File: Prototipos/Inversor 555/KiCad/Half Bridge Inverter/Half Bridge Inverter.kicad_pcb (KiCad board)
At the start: 2 copper layers, 91 x 53.5 mm, 15 parts, among them Q1 CSD18534Q5A, Q2 CSD18534Q5A, Q3 BC548, U1 TLC555xD, U2 LM7809_TO220

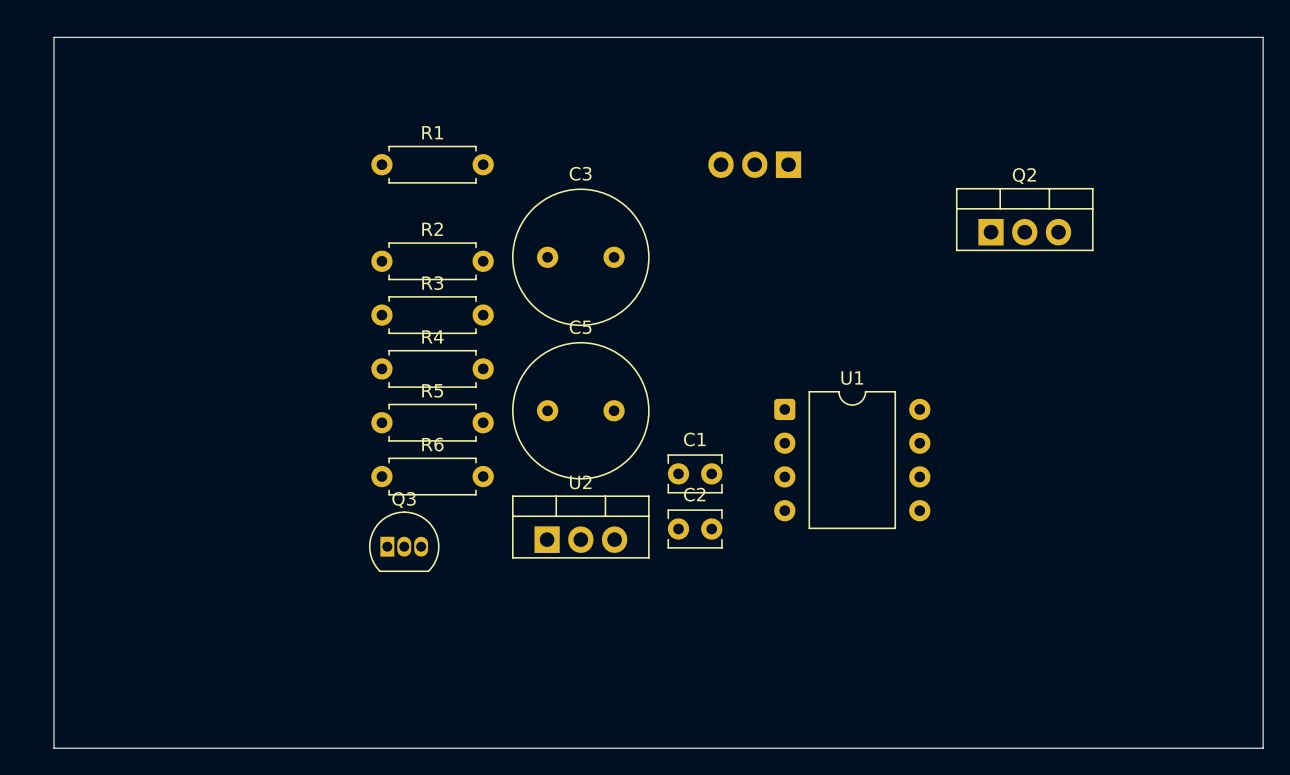
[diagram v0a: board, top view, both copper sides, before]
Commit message: Agregar diseño PCB
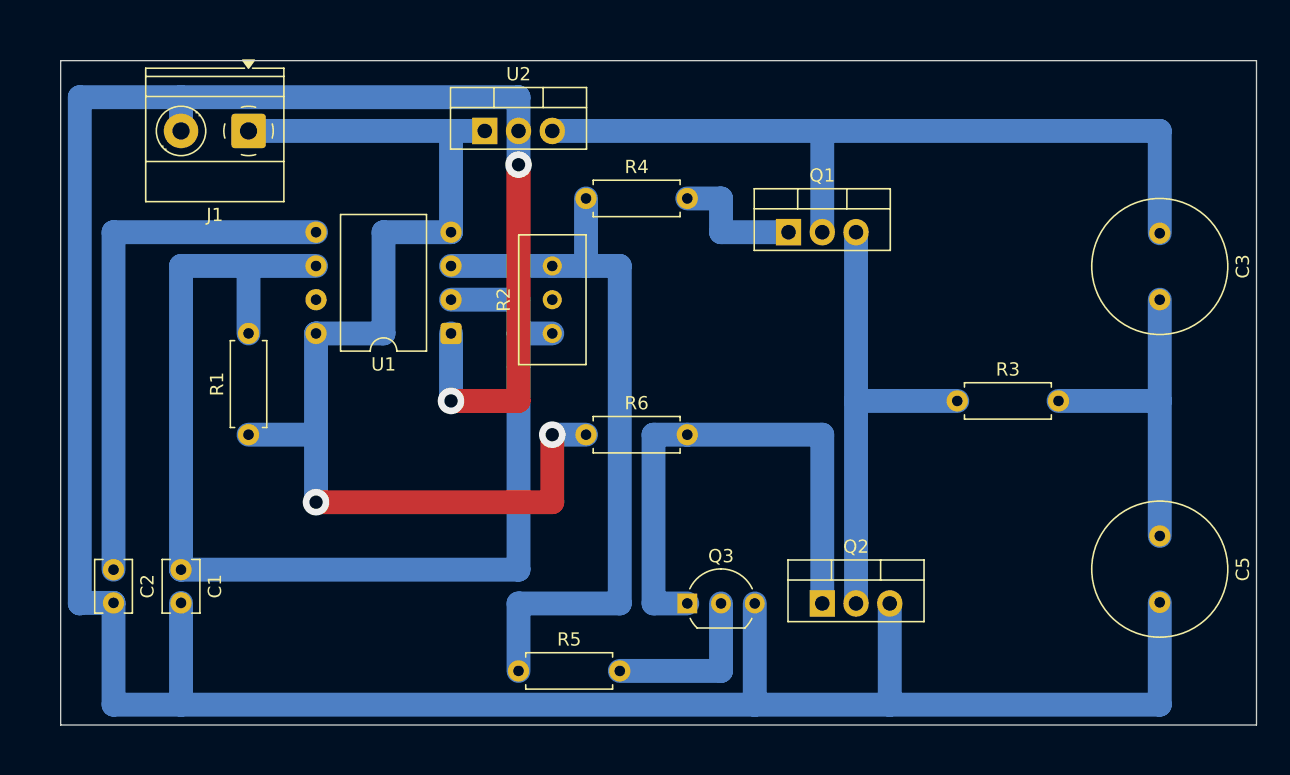
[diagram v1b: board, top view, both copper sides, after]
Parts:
- added J1: Screw_Terminal_01x02, TerminalBlock_Phoenix:TerminalBlock_Phoenix_MKDS-1,5-2-5.08_1x02_P5.08mm_Horizontal, F.Cu at (104.1, 66.0)
- Q1: value CSD18534Q5A -> IRF4905; moved to F.Cu
- Q2: value CSD18534Q5A -> IRF4905
- Q3: footprint Package_TO_SOT_THT:TO-92_Inline -> Package_TO_SOT_THT:TO-92_Inline_Wide
- R2: footprint Resistor_THT:R_Axial_DIN0207_L6.3mm_D2.5mm_P7.62mm_Horizontal -> Potentiometer_THT:Potentiometer_Bourns_3296W_Vertical
- moved C5 47.0 mm to (172.7, 96.5), turned to -90 degrees
- moved C3 46.1 mm to (172.7, 73.7), turned to -90 degrees
- moved R3 43.8 mm to (157.5, 86.4)
- moved C2 42.6 mm to (94.0, 99.1), turned to -90 degrees
- moved C1 38.1 mm to (99.1, 99.1), turned to -90 degrees
- moved U2 31.1 mm to (121.9, 66.0)
- moved Q2 30.7 mm to (147.3, 101.6)
- moved U1 25.8 mm to (119.4, 81.3), turned to 180 degrees
- moved Q3 23.0 mm to (137.2, 101.6)
- moved R1 22.7 mm to (104.1, 88.9), turned to 90 degrees
- moved R5 21.3 mm to (124.5, 106.7)
- moved R4 20.0 mm to (129.5, 71.1)
- moved R6 15.7 mm to (129.5, 88.9)
- moved R2 12.8 mm to (127.0, 76.2), turned to 90 degrees
- moved Q1 5.08 mm to (144.8, 73.7), turned to 0 degrees
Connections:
- Q1 pad 1: Net-(Q2-D) -> Net-(Q1-G)
- Q1 pad 2: Net-(Q2-D) -> Net-(Q1-D)
- Q1 pad 3: Net-(Q2-D) -> Net-(Q1-S)
- Q2 pad 1: Earth -> Net-(Q2-G)
- Q2 pad 2: Earth -> Net-(Q1-S)
- R2 pad 2: Net-(U1-THR) -> (no net)
- R3 pad 1: Net-(Q2-D) -> Net-(Q1-S)
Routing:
- net Earth: track 0.00 -> 226.2 mm, vias 0 -> 2
- net Net-(U1-THR): track 0.00 -> 91.4 mm
- net VDD: track 0.00 -> 86.4 mm, vias 0 -> 2
- net Net-(Q1-D): track 0.00 -> 61.0 mm
- net 555: track 0.00 -> 55.9 mm
- net Net-(U1-CV): track 0.00 -> 40.6 mm
- net Net-(Q2-G): track 0.00 -> 40.6 mm
- net Net-(Q1-S): track 0.00 -> 35.6 mm
- net Net-(C3-Pad2): track 0.00 -> 25.4 mm
- net Net-(Q3-B): track 0.00 -> 12.7 mm
- net Net-(Q1-G): track 0.00 -> 10.2 mm
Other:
- board size 91 x 53.5 mm -> 90 x 50 mm

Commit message: Modificaciones varias para facilitar visualización
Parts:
- U1: footprint Package_DIP:DIP-8_W10.16mm -> Package_DIP:DIP-8_W7.62mm
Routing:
- net Net-(U1-THR): track 91.4 -> 94.0 mm, vias 0 -> 58
- net Net-(U1-CV): track 40.6 -> 43.2 mm, vias 0 -> 18
- net unconnected-(U1-NC-Pad5): vias 0 -> 2
- net unconnected-(U1-NC-Pad3): vias 0 -> 2
- net unconnected-(U1-DIS-Pad7): vias 0 -> 2
- net VDD: vias 2 -> 38
- net UC_RELAY: vias 0 -> 2
- net UC_PHASE: vias 0 -> 7
- net UC_DOUT: vias 0 -> 4
- net Retro_micro: vias 0 -> 1
- net RELAY_T2: vias 0 -> 4
- net PWM_micro: vias 0 -> 2
- net PWM_BJT: vias 0 -> 1
- net Net-(R7-Pad2): vias 0 -> 10
- net Net-(R5-Pad2): vias 0 -> 4
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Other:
- board size 90 x 50 mm -> 90 x 52.5 mm
- board text added: "1"
- board text added: "10"
- board text added: "11"
- board text added: "12"
- board text added: "13"
- board text added: "14"
- board text added: "15"
- board text added: "16"
- board text added: "17"
- board text added: "18"
- board text added: "19"
- board text added: "2"
- board text added: "3"
- board text added: "4"
- board text added: "5"
- board text added: "6"
- board text added: "7"
- board text added: "8"
- board text added: "9"
- board text added: "A"
- board text added: "B"
- board text added: "C"
- board text added: "D"
- board text added: "E"
- board text added: "F"
- board text added: "G"
- board text added: "H"
- board text added: "I"
- board text added: "J"
- board text added: "K"
- board text added: "L"
- board text added: "M"
- board text added: "N"
- board text added: "O"
- board text added: "P"
- board text added: "Q"
- board text added: "R"
- board text added: "S"
- board text added: "T"
- board text added: "V"
- board text added: "W"
- board text added: "X"
- board text added: "Y"
- board text added: "Z"
